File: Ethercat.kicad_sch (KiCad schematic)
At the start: 51 parts, among them J1 RJ45_Amphenol_RJMG1BD3B8K1ANR, J2 RJ45_Amphenol_RJMG1BD3B8K1ANR, Y1 LFXTAL085880

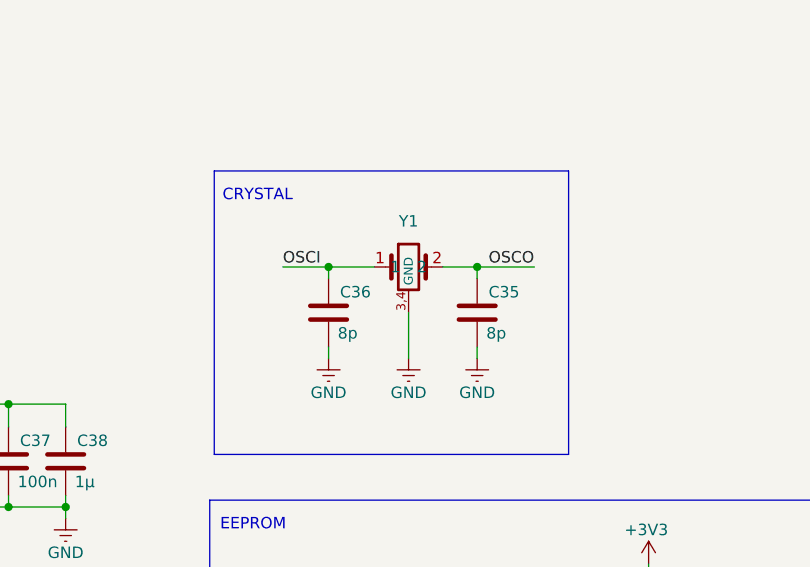
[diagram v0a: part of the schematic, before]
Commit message: power
power ic for 12V->3.3V implemented
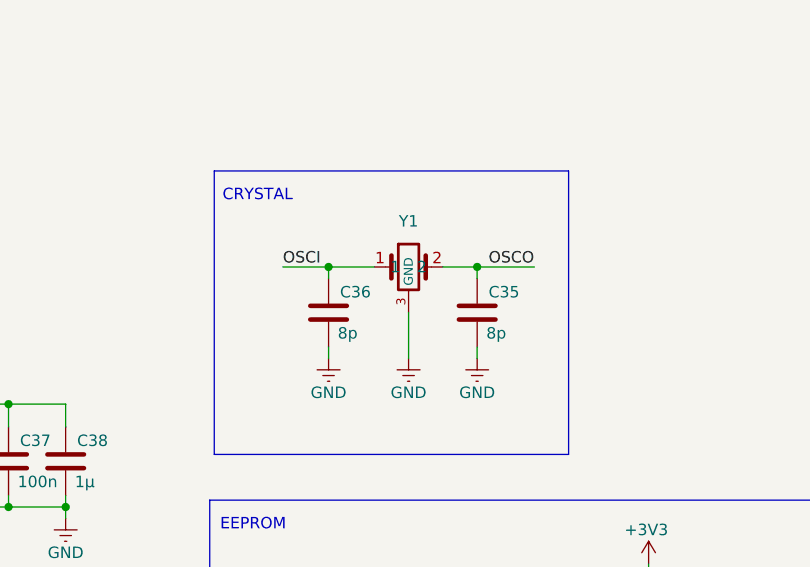
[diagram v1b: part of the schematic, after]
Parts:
- removed Y1: LFXTAL085880, Crystals:LFXTAL085880, symbol Oscillators:25Mhz_crystal
- added Y1: LFXTAL085880, Footprintsymbolen_samen:25Mhz crystal 8pF, symbol Symbolen_samen:25Mhz_crystal
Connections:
- net GND: now also Y1.3 (GND)
- net OSCI: now also Y1.1
- net OSCO: now also Y1.2
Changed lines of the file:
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@@
 	)
 	(symbol
+		(lib_id "Symbolen_samen:25Mhz_crystal")
+		(at 264.16 134.62 0)
+		(unit 1)
+		(body_style 1)
+		(exclude_from_sim no)
+		(in_bom yes)
+		(on_board yes)
+		(in_pos_files yes)
+		(dnp no)
+		(fields_autoplaced yes)
+		(property "Reference" "Y1"
+			(at 267.97 130.81 0)
+			(show_name no)
+			(do_not_autoplace no)
+			(effects
+				(font
+					(size 1.27 1.27)
+				)
+			)
+		)
+		(property "Value" "LFXTAL085880"
+			(at 255.524 127 0)
+			(hide yes)
+			(show_name no)
+			(do_not_autoplace no)
+			(effects
+				(font
+					(size 1.27 1.27)
+				)
+			)
+		)
+		(property "Footprint" "Footprintsymbolen_samen:25Mhz crystal 8pF"
+			(at 259.588 124.206 0)
+			(hide yes)
+			(show_name no)
+			(do_not_autoplace no)
+			(effects
+				(font
+					(size 1.27 1.27)
+				)
+			)
+		)
+		(property "Datasheet" "https://www.mouser.be/datasheet/3/1460/1/LFXTAL085880.pdf"
+			(at 280.162 129.032 0)
+			(hide yes)
+			(show_name no)
+			(do_not_autoplace no)
+			(effects
+				(font
+					(size 1.27 1.27)
+				)
+			)
+		)
+		(property "Description" ""
+			(at 264.16 134.62 0)
+			(hide yes)
+			(show_name no)
+			(do_not_autoplace no)
+			(effects
+				(font
+					(size 1.27 1.27)
+				)
+			)
+		)
+		(pin "4"
+		)
+		(pin "2"
+		)
+		(pin "3"
+		)
+		(pin "1"
+		)
+		(instances
+			(project "ESC_PLC"
+				(path "/5bd3bb6f-fe53-443c-806c-077e2bbb5d14/f038ea58-2b1a-4d87-b3c8-8d32ce4ec05b"
+					(reference "Y1")
+					(unit 1)
+				)
+			)
+		)
+	)
+	(symbol
 		(lib_id "power:+3V3")
 		(at 175.26 226.06 0)
@@
 					(unit 1)
 				)
-			)
-		)
-	)
-	(symbol
-		(lib_id "Oscillators:25Mhz_crystal")
-		(at 264.16 134.62 0)
-		(unit 1)
-		(body_style 1)
-		(exclude_from_sim no)
-		(in_bom yes)
-		(on_board yes)
-		(in_pos_files yes)
-		(dnp no)
-		(fields_autoplaced yes)
-		(property "Reference" "Y1"
-			(at 267.97 130.81 0)
-			(show_name no)
-			(do_not_autoplace no)
-			(effects
-				(font
-					(size 1.27 1.27)
-				)
-			)
-		)
-		(property "Value" "LFXTAL085880"
-			(at 255.524 127 0)
-			(hide yes)
-			(show_name no)
-			(do_not_autoplace no)
-			(effects
-				(font
-					(size 1.27 1.27)
-				)
-			)
-		)
-		(property "Footprint" "Crystals:LFXTAL085880"
-			(at 259.588 124.206 0)
-			(hide yes)
-			(show_name no)
-			(do_not_autoplace no)
-			(effects
-				(font
-					(size 1.27 1.27)
-				)
-			)
-		)
-		(property "Datasheet" "https://www.mouser.be/datasheet/3/1460/1/LFXTAL085880.pdf"
-			(at 280.162 129.032 0)
-			(hide yes)
-			(show_name no)
-			(do_not_autoplace no)
-			(effects
-				(font
-					(size 1.27 1.27)
-				)
-			)
-		)
-		(property "Description" ""
-			(at 264.16 134.62 0)
-			(hide yes)
-			(show_name no)
-			(do_not_autoplace no)
-			(effects
-				(font
-					(size 1.27 1.27)
-				)
-			)
-		)
-		(pin "2"
-		)
-		(pin "1"
-		)
-		(pin "3,4"
-		)
-		(instances
-			(project "ESC_PLC"
-				(path "/5bd3bb6f-fe53-443c-806c-077e2bbb5d14/f038ea58-2b1a-4d87-b3c8-8d32ce4ec05b"
-					(reference "Y1")
-					(unit 1)
-				)

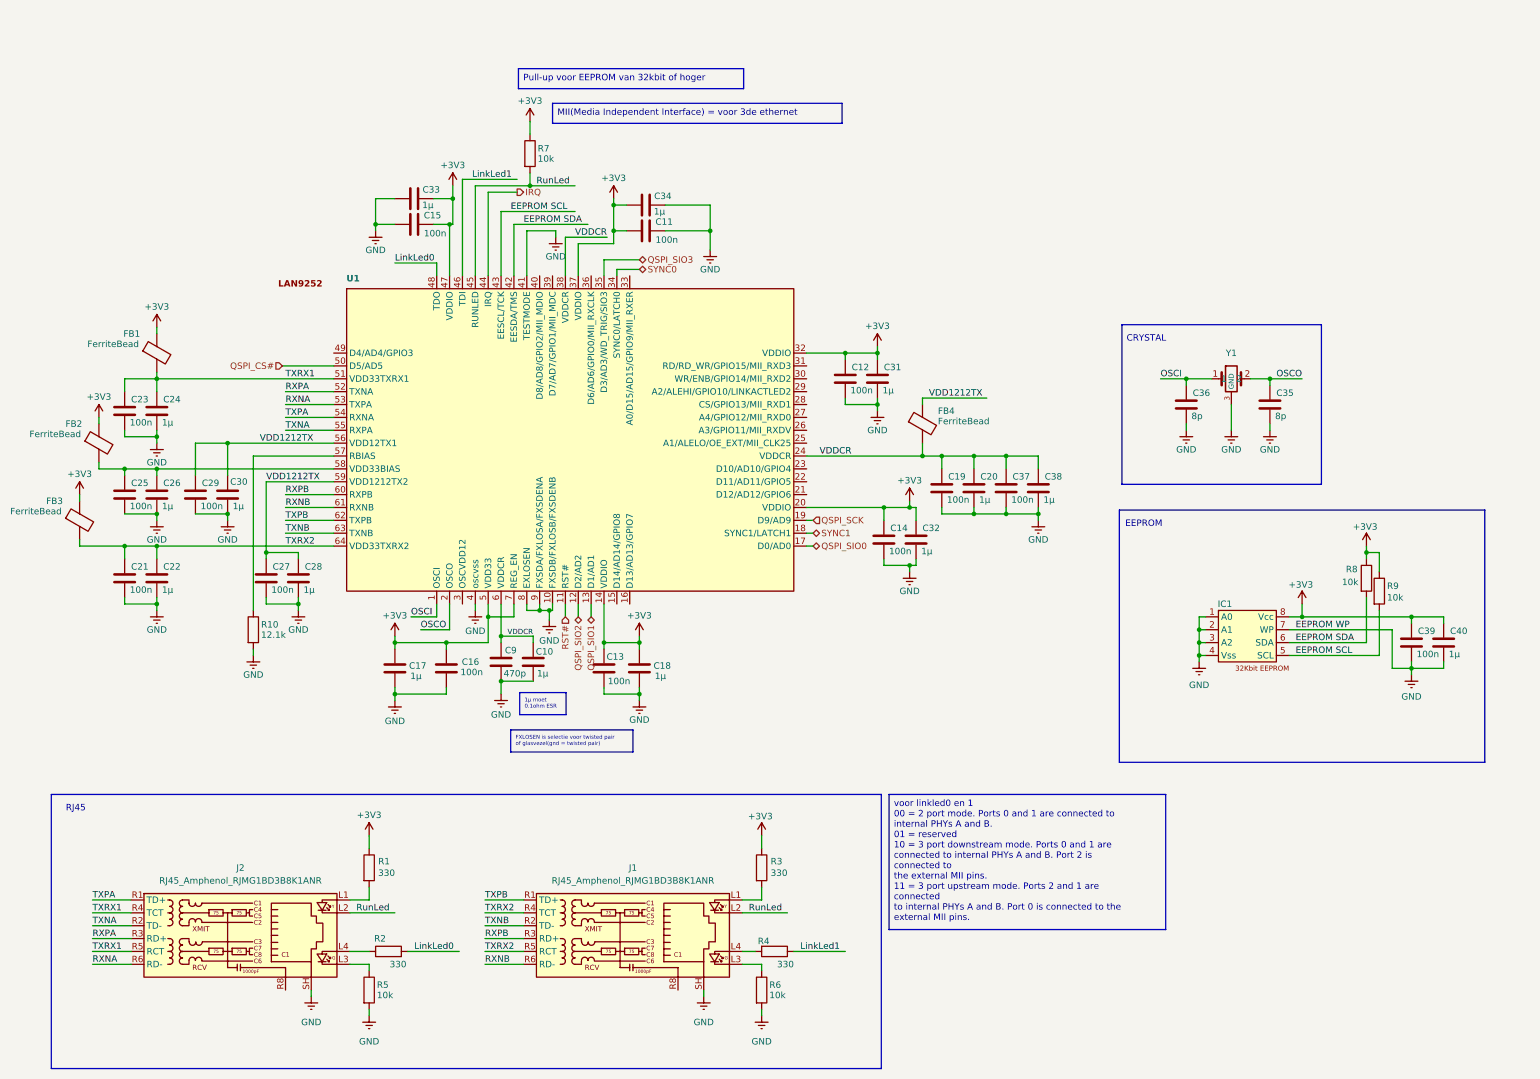
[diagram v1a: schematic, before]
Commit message: footprints
footprints aan de condensators toegevoegd
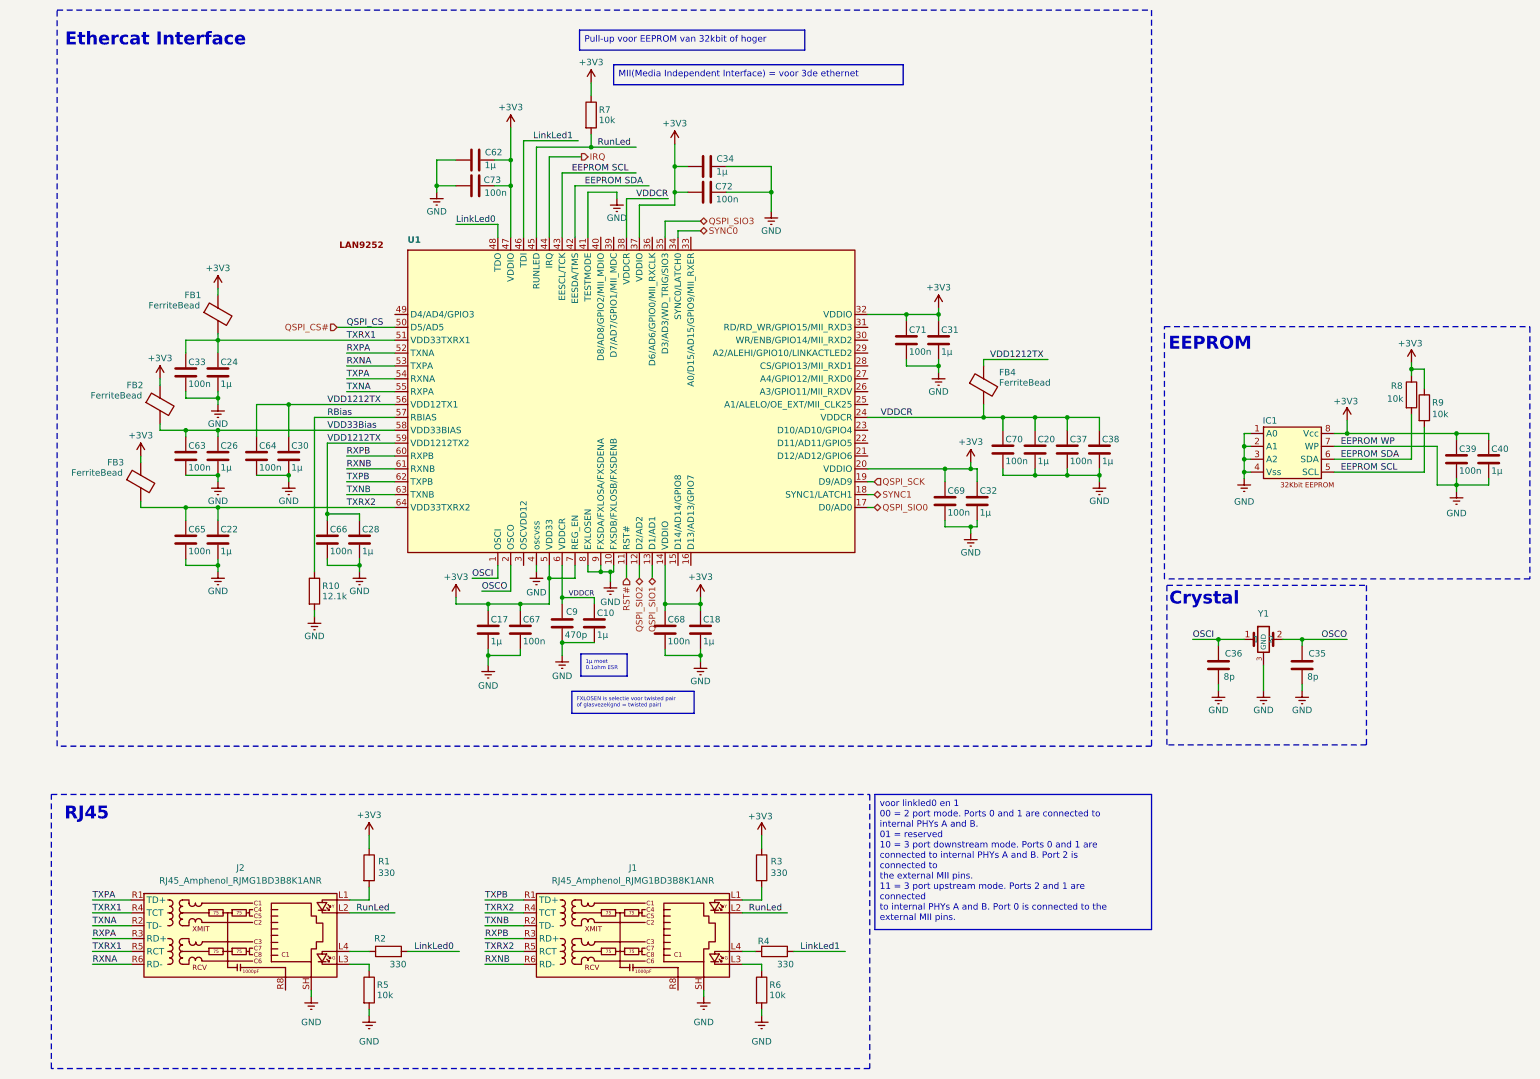
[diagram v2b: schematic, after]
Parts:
- removed C11, C12, C13, C14, C15, C16, C19, C21, C23, C25, C27, C29: 100n, EEPROM:579-24LC32AFT-ISN, symbol Device:C
- added C62: 1µ, Capacitor_SMD:C_0603_1608Metric, symbol Device:C
- added C63, C64, C65, C66, C67, C68, C69, C70, C71, C72, C73: 100n, Capacitor_SMD:C_0603_1608Metric, symbol Device:C
- C10, C17, C18, C20, C22, C24, C26, C28, C30, C31, C32, C34, C37, C38, C39, C40, C9: footprint EEPROM:579-24LC32AFT-ISN -> Capacitor_SMD:C_0603_1608Metric
- C33: value 1µ -> 100n; footprint EEPROM:579-24LC32AFT-ISN -> Capacitor_SMD:C_0603_1608Metric
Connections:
- net +3V3: now also C62.2, C67.1, C68.1, C69.1, C71.1, C72.1, C73.2; no longer C33.2
- net GND: now also C33.2, C62.1, C63.2, C64.2, C65.2, C66.2, C67.2, C68.2, C69.2, C70.2, C71.2, C72.2, C73.1; no longer C33.1
- net TXRX1: now also C33.1
- net TXRX2: now also C65.1
- net VDD1212TX: now also C64.1, C66.1
- net VDDCR: now also C70.1
- net VDD33Bias: now reaches C26.1, FB2.2, U1.58 (VDD33BIAS)
- net VDD33Bias: now also C63.1
- net RBias: now reaches R10.1, U1.57 (RBIAS)
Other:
- note added: "Crystal"
- note added: "Ethercat Interface"
- note removed: "CRYSTAL"
- moved on the sheet: C35, C36, C9, FB1, FB2, FB3, FB4, IC1, R10, R7, R8, R9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

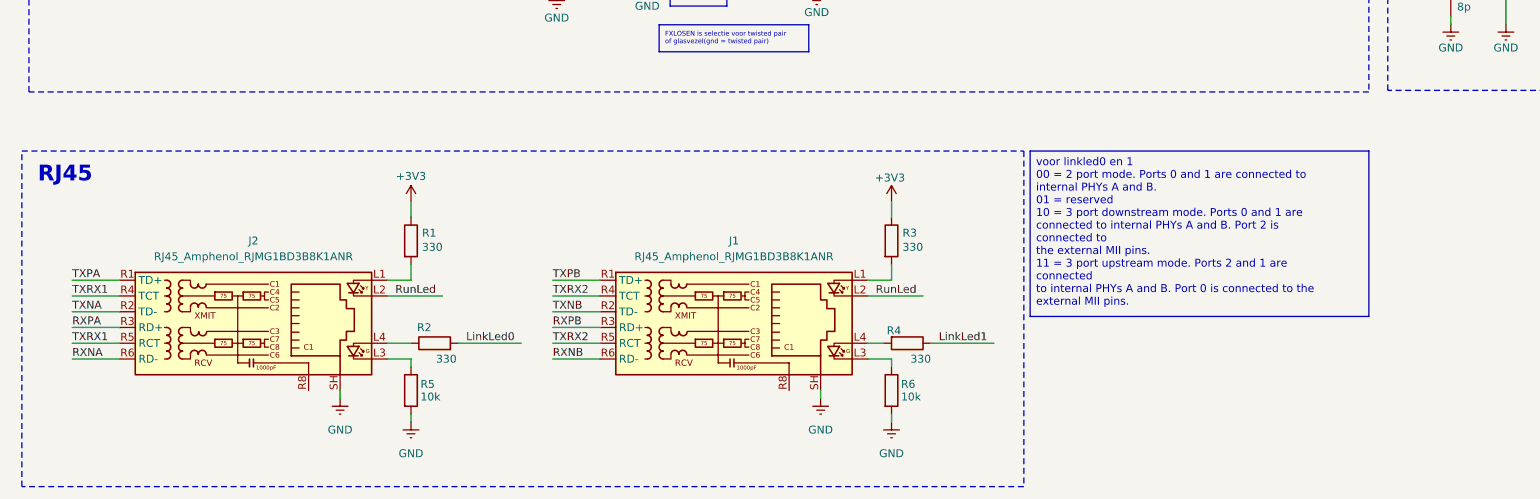
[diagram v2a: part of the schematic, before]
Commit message: BLDC en 5V
bldc motor aangesloten alsook 5V gemaakt
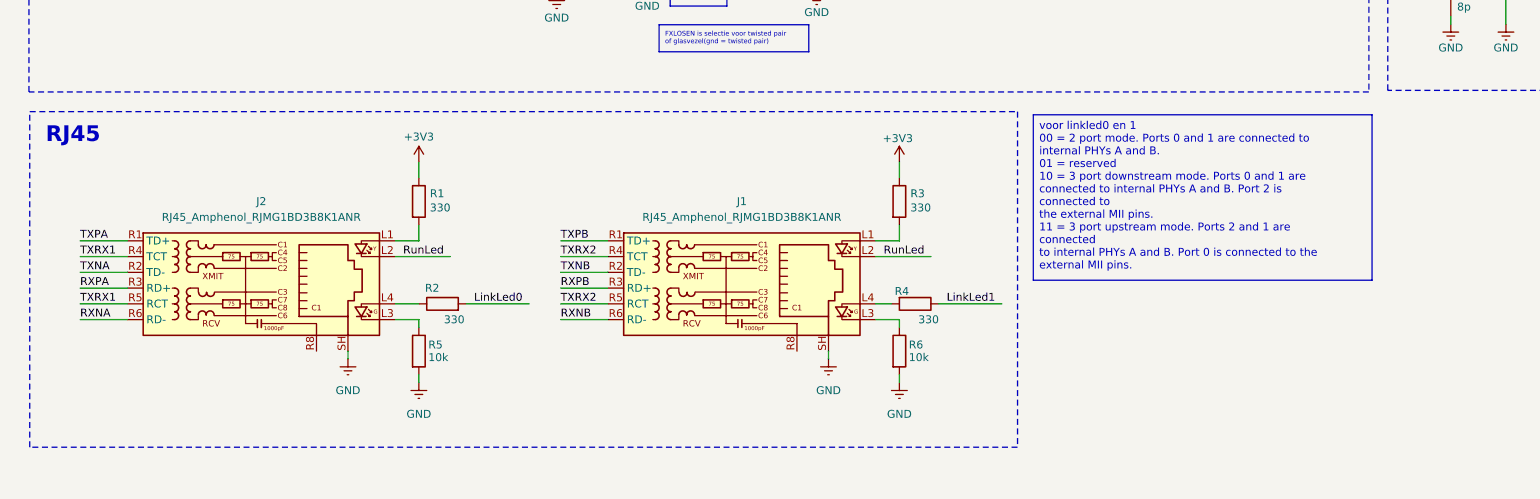
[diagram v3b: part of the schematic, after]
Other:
- moved on the sheet: J1, J2, R1, R2, R3, R4, R5, R6

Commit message: schemas klaar
schemas en footprints aan symbolen allemaal juist gemaakt
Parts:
- removed FB3: FerriteBead, Package_LCC:PLCC-84_29.3x29.3mm_P1.27mm, symbol Device:FerriteBead
- removed U1: (no value), Package_QFP:LQFP-100_14x14mm_P0.5mm, symbol Ethercat:LAN9252
- removed Y1: LFXTAL085880, Footprintsymbolen_samen:25Mhz crystal 8pF, symbol Symbolen_samen:25Mhz_crystal
- added FB1: FerriteBead, Footprintsymbolen_samen:Ferrite Bead 0603, symbol Device:FerriteBead
- added U2: (no value), Footprintsymbolen_samen:LAN9252, symbol Schemasymbolen_samen:LAN9252
- added Y1: LFXTAL085880, Footprintsymbolen_samen:25Mhz crystal 8pF, symbol Schemasymbolen_samen:25Mhz_crystal
- C43: renamed from C36; footprint EEPROM:579-24LC32AFT-ISN -> Capacitor_SMD:C_0603_1608Metric
- C44: renamed from C35; footprint EEPROM:579-24LC32AFT-ISN -> Capacitor_SMD:C_0603_1608Metric
- FB2, FB4: footprint Package_LCC:PLCC-84_29.3x29.3mm_P1.27mm -> Footprintsymbolen_samen:Ferrite Bead 0603
- FB3: renamed from FB1; footprint Package_LCC:PLCC-84_29.3x29.3mm_P1.27mm -> Footprintsymbolen_samen:Ferrite Bead 0603
- IC1: footprint EEPROM:579-24LC32AFT-ISN -> Footprintsymbolen_samen:EEPROM 32Kbit
- R1: renamed from R10; footprint (none) -> Resistor_SMD:R_0603_1608Metric
- R10: renamed from R9; footprint (none) -> Resistor_SMD:R_0603_1608Metric
- R2: renamed from R1; footprint Connector_RJ:RJ45_Amphenol_RJMG1BD3B8K1ANR -> Resistor_SMD:R_0603_1608Metric
- R3: renamed from R5; footprint (none) -> Resistor_SMD:R_0603_1608Metric
- R4: renamed from R2; footprint (none) -> Resistor_SMD:R_0603_1608Metric
- R5: renamed from R7; footprint (none) -> Resistor_SMD:R_0603_1608Metric
- R6: renamed from R3; footprint Connector_RJ:RJ45_Amphenol_RJMG1BD3B8K1ANR -> Resistor_SMD:R_0603_1608Metric
- R7: renamed from R6; footprint (none) -> Resistor_SMD:R_0603_1608Metric
- R8: renamed from R4; footprint (none) -> Resistor_SMD:R_0603_1608Metric
- R9: renamed from R8; footprint (none) -> Resistor_SMD:R_0603_1608Metric
- renumbered C33 to C15, C63 to C16, C65 to C17, C24 to C18, C26 to C19, C22 to C20, C64 to C21, C30 to C22, C66 to C23, C28 to C24, C62 to C25, C73 to C26, C17 to C27, C67 to C28, C9 to C29, C10 to C30, C68 to C31, C18 to C32, C34 to C33, C72 to C34, C71 to C35, C31 to C36, C69 to C37, C32 to C38, C70 to C39, C20 to C40, C37 to C41, C38 to C42, C39 to C45, C40 to C46, J2 to J1, J1 to J2
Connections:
- net +3V3: now also FB1.1, U2.14 (VDDIO), U2.20 (VDDIO), U2.32 (VDDIO), U2.37 (VDDIO), U2.47 (VDDIO), U2.5 (VDD33), U2.7 (REG_EN)
- net EEPROM SCL: now also U2.43 (EESCL/TCK)
- net EEPROM SDA: now also U2.42 (EESDA/TMS)
- net GND: now also U2.10 (FXSDB/FXLOSB/FXSDENB), U2.4 (oscvss), U2.41 (TESTMODE), U2.8 (EXLOSEN), U2.9 (FXSDA/FXLOSA/FXSDENA), Y1.2 (GND)
- net IRQ: now also U2.44 (IRQ)
- net LinkLed0: now also U2.48 (TDO)
- net LinkLed1: now also U2.46 (TDI)
- net OSCI: now also U2.1 (OSCI), Y1.1
- net OSCO: now also U2.2 (OSCO), Y1.3
- net QSPI_CS#: now also U2.50 (D5/AD5)
- net QSPI_SCK: now also U2.19 (D9/AD9)
- net QSPI_SIO0: now also U2.17 (D0/AD0)
- net QSPI_SIO1: now also U2.13 (D1/AD1)
- net QSPI_SIO2: now also U2.12 (D2/AD2)
- net QSPI_SIO3: now also U2.35 (D3/AD3/WD_TRIG/SIO3)
- net RBias: now also U2.57 (RBIAS)
- net RST#: now also U2.11 (RST#)
- net RXNA: now also U2.53 (TXPA)
- net RXNB: now also U2.61 (RXNB)
- net RXPA: now also U2.52 (TXNA)
- net RXPB: now also U2.60 (RXPB)
- net RunLed: now also U2.45 (RUNLED)
- net SYNC0: now also U2.34 (SYNC0/LATCH0)
- net SYNC1: now also U2.18 (SYNC1/LATCH1)
- net TXNA: now also U2.55 (RXPA)
- net TXNB: now also U2.63 (TXNB)
- net TXPA: now also U2.54 (RXNA)
- net TXPB: now also U2.62 (TXPB)
- net TXRX1: now also U2.51 (VDD33TXRX1)
- net TXRX2: now also FB1.2, U2.64 (VDD33TXRX2)
- net VDD1212TX: now also U2.56 (VDD12TX1), U2.59 (VDD1212TX2)
- net VDD33Bias: now also U2.58 (VDD33BIAS)
- net VDDCR: now also U2.24 (VDDCR), U2.38 (VDDCR), U2.6 (VDDCR)

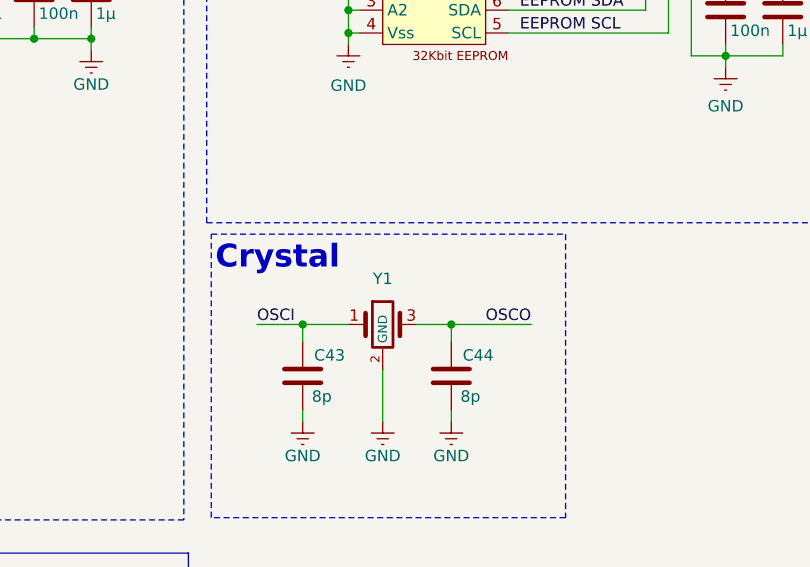
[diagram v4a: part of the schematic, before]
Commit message: pcb gesorteerd
al de main blokken bij elkaar gezet
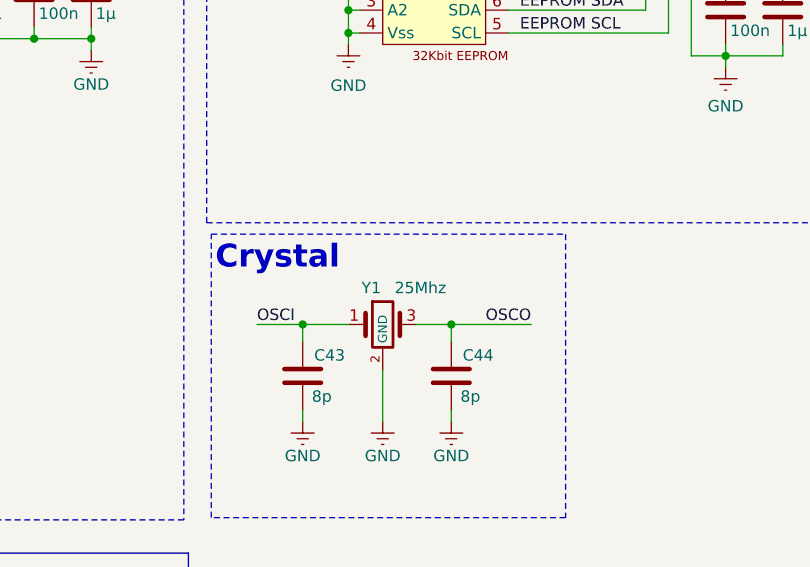
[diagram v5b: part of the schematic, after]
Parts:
- Y1: value LFXTAL085880 -> 25Mhz
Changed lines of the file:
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@@
 		(in_pos_files yes)
 		(dnp no)
-		(fields_autoplaced yes)
 		(property "Reference" "Y1"
-			(at 274.32 181.61 0)
+			(at 273.05 182.626 0)
 			(show_name no)
 			(do_not_autoplace no)
@@
 			)
 		)
-		(property "Value" "LFXTAL085880"
-			(at 261.874 177.8 0)
-			(hide yes)
+		(property "Value" "25Mhz"
+			(at 278.511 182.626 0)
 			(show_name no)
 			(do_not_autoplace no)
@@
 			)
 		)
-		(property "Description" ""
+		(property "Description" "LFXTAL085880"
 			(at 270.51 185.42 0)
 			(hide yes)
